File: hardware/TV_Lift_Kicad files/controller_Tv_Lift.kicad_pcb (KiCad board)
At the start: 4 copper layers, 70 x 157.5 mm, 96 parts, among them J1 socket LAN8720a, J10 CONN_IR_OUT, J11 DRY CONTACT UP DOWN, J12 DRY CONTACT, J2 POWER 24V, J3 CAN_bus, J4 ENCODER, J5 ENCODER_POWER, J6 CONN_RS232, J7 M1 LIMIT UP DOWN, J8 Signal PWR, J9 MOTOR_OUT, Q1 2N3904, SW1 UP, SW2 DOWN, SW3 STOP, U1 MAX3232, U10 VNH5019A-E, U2 TSOP32S40F, U3 SN65HVD230, U4 ESP32-WROOM-32, U5 LM2596S-5, U6 AMS1117-3.3, U7 PC817, U8 PC817, U9 NCS1S1205SC

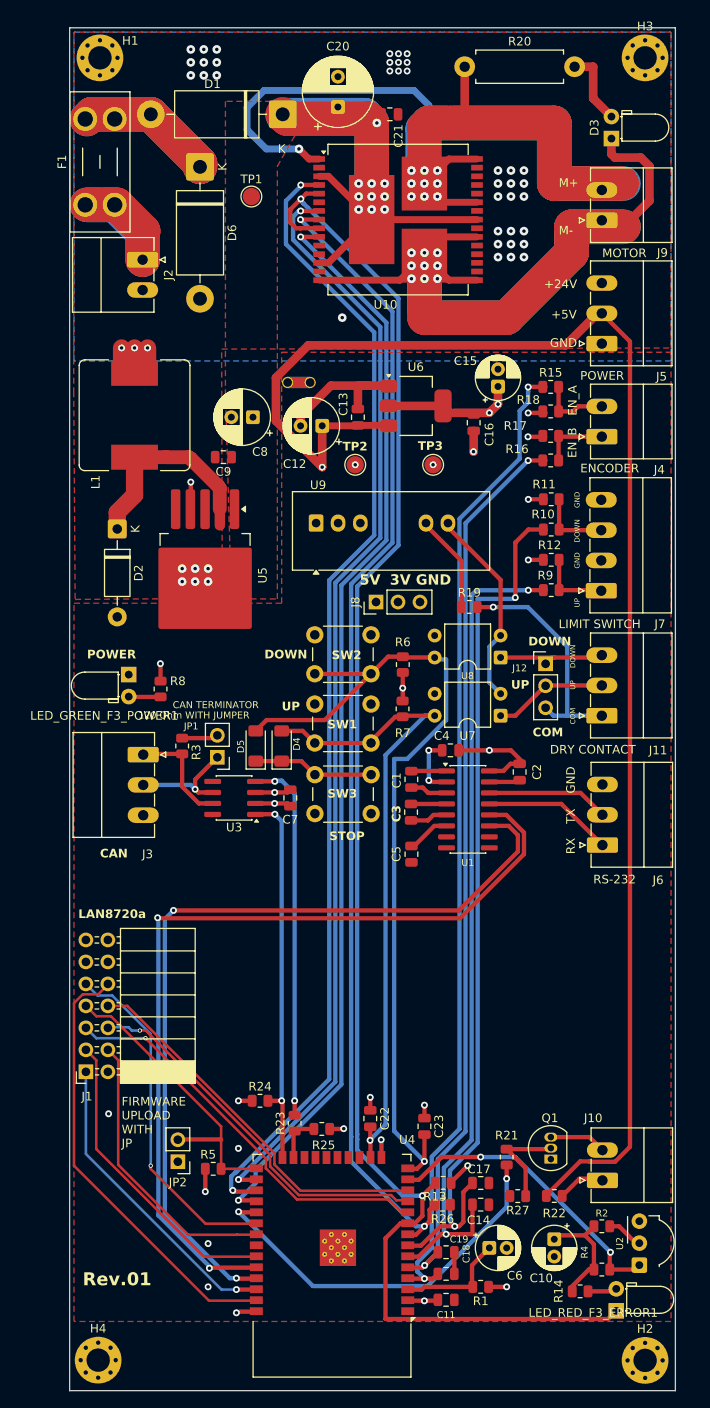
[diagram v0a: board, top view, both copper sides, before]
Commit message: fix schema ( fuse + annotation)
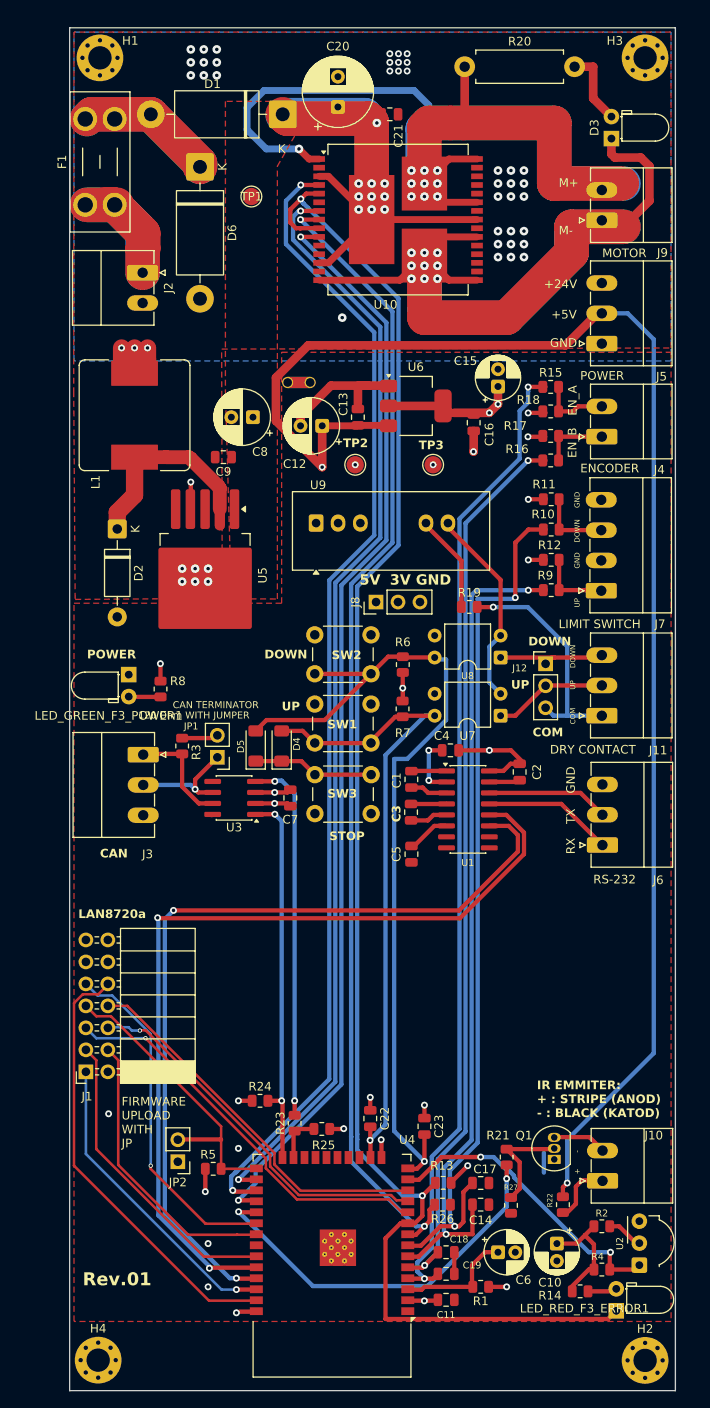
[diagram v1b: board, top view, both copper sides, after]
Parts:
- moved J2 1.50 mm to (73.9, 53.8)
- moved R22 1.41 mm to (122.5, 161.5), turned to -90 degrees
- moved R27 1.33 mm to (116.5, 161.6), turned to -90 degrees
- moved C6 1.12 mm to (115.0, 167.0)
- moved C10 0.59 mm to (121.8, 166.0)
- moved Q1 0.40 mm to (121.5, 156.3)
- moved J10 0.06 mm to (127.1, 158.8)
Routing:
- net Net-(J2-Pin_1): track 34.1 -> 38.7 mm
- net Net-(J10-Pin_2): track 6.58 -> 9.22 mm
- net Net-(J10-Pin_1): track 5.56 -> 7.05 mm
- net +5V: track 187.5 -> 188.4 mm, vias 6 -> 7
- net Net-(U4-EN): track 13.0 -> 13.8 mm
- net +3.3V: track 71.9 -> 72.4 mm
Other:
- board text added: "+"
- board text added: "-"
- board text added: "IR EMMITER: + : STRIPE (ANOD) - : BLACK (KATOD)"

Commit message: fix annotations on sockets output
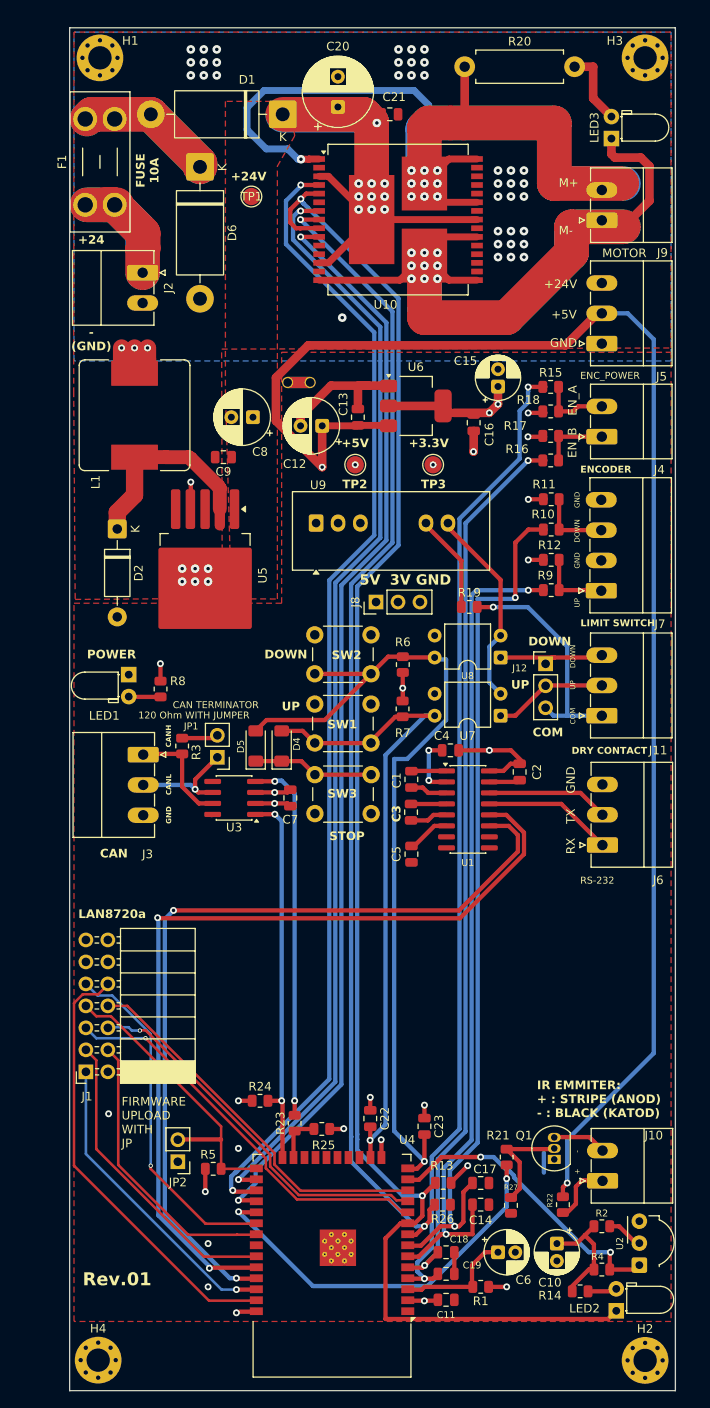
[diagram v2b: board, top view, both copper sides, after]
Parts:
- F1: value Fuse_Small -> Fuse_Mini_10A
- LED1: renamed from LED_GREEN_F3_POWER1; value LED -> LED_GREEN_F3
- LED2: renamed from LED_RED_F3_ERROR1; value LED_ERROR -> LED_RED_F3
- renumbered D3 to LED3
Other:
- board text added: "+24"
- board text added: "+3.3V"
- board text added: "- (GND)"
- board text added: "CANH"
- board text added: "CANL"
- board text added: "ENC_POWER"
- board text added: "FUSE 10A"

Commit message: add button reset
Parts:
- added SW4: Reset, Button_Switch_THT:SW_PUSH_6mm, F.Cu at (67.5, 173.2)
- D1: value 1N5822 -> 80SQ045
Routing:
- net Net-(U4-EN): track 13.8 -> 57.2 mm, vias 0 -> 1
- net Net-(J10-Pin_2): track 9.22 -> 6.92 mm
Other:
- board text added: "Reset"

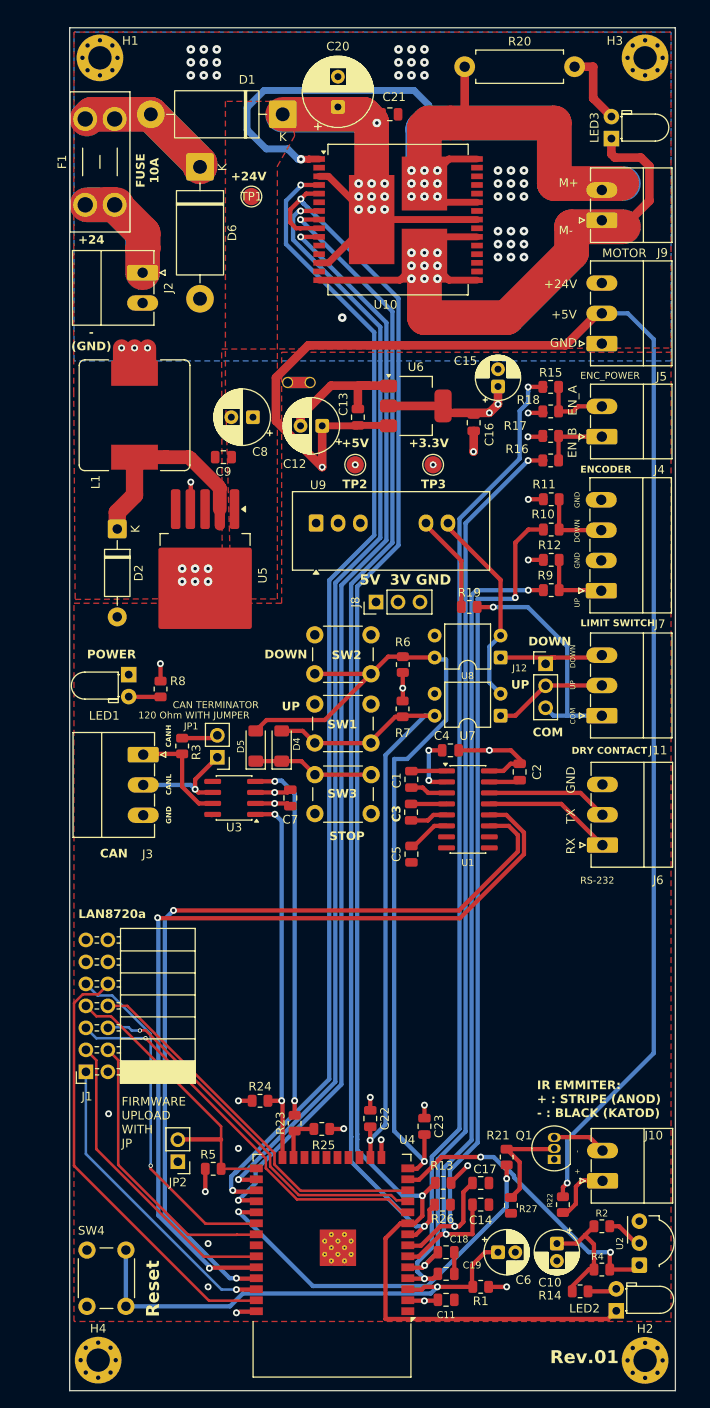
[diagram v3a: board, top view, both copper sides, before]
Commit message: add ground poligon on bottom layer
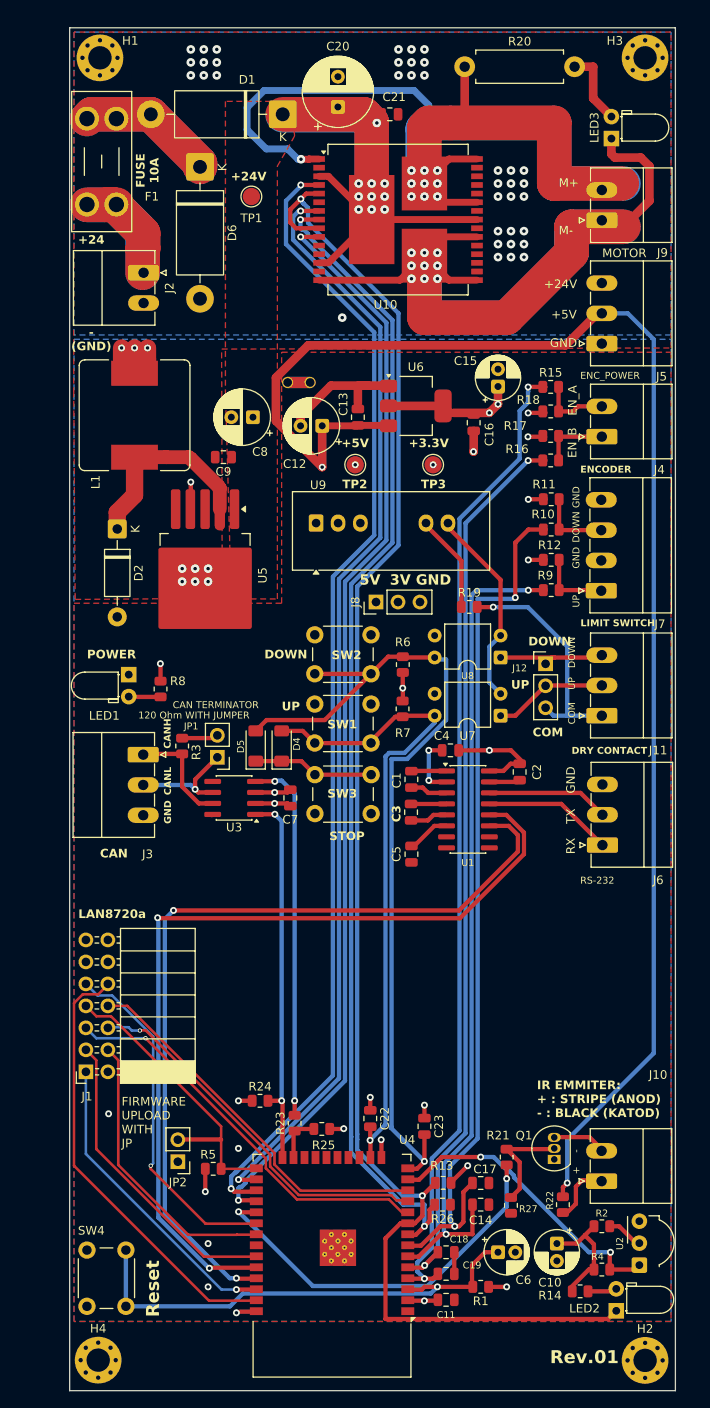
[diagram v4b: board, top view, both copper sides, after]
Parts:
- moved F1 0.20 mm to (67.5, 45.9)
- moved J10 0.11 mm to (127.0, 158.8)
- moved J2 0.11 mm to (74.0, 53.8)
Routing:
- net /M1_CS: track 134.3 -> 135.3 mm
- added copper zone on B.Cu, net GND

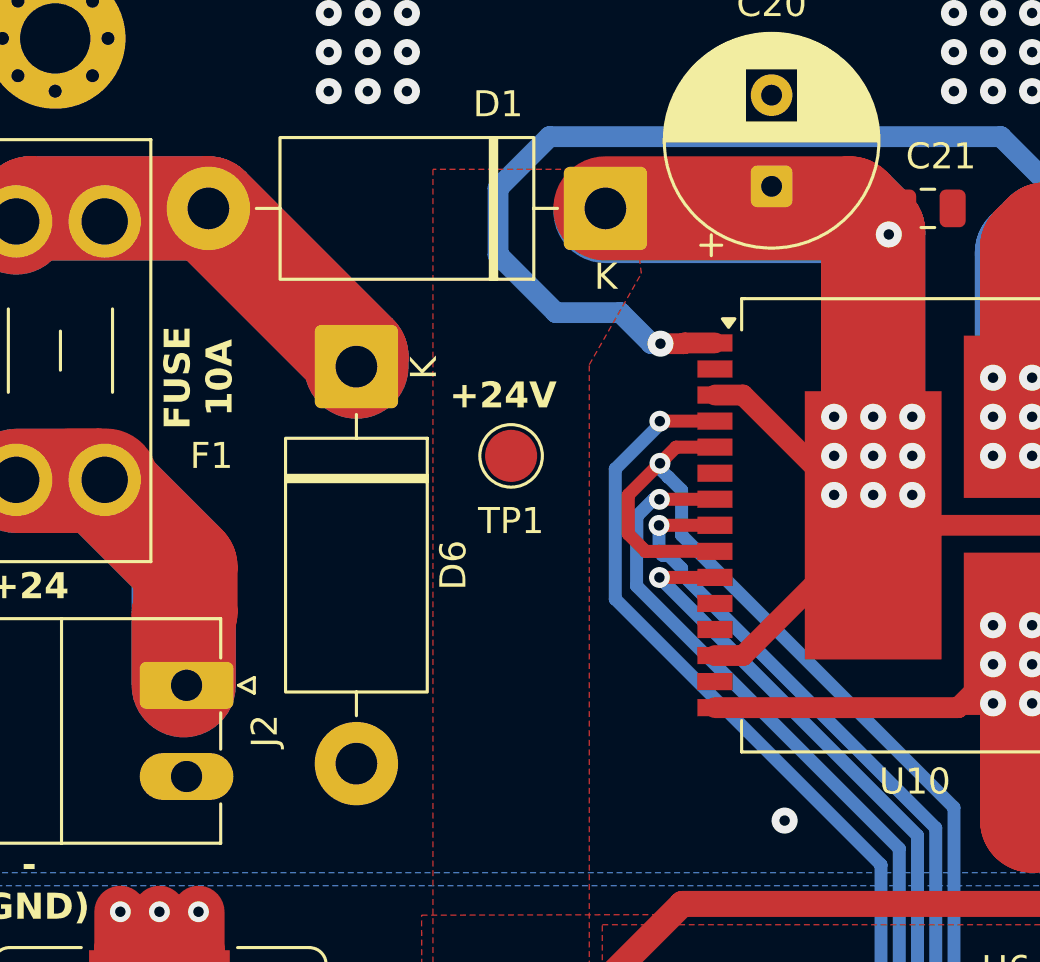
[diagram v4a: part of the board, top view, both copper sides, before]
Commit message: change diod suspressor
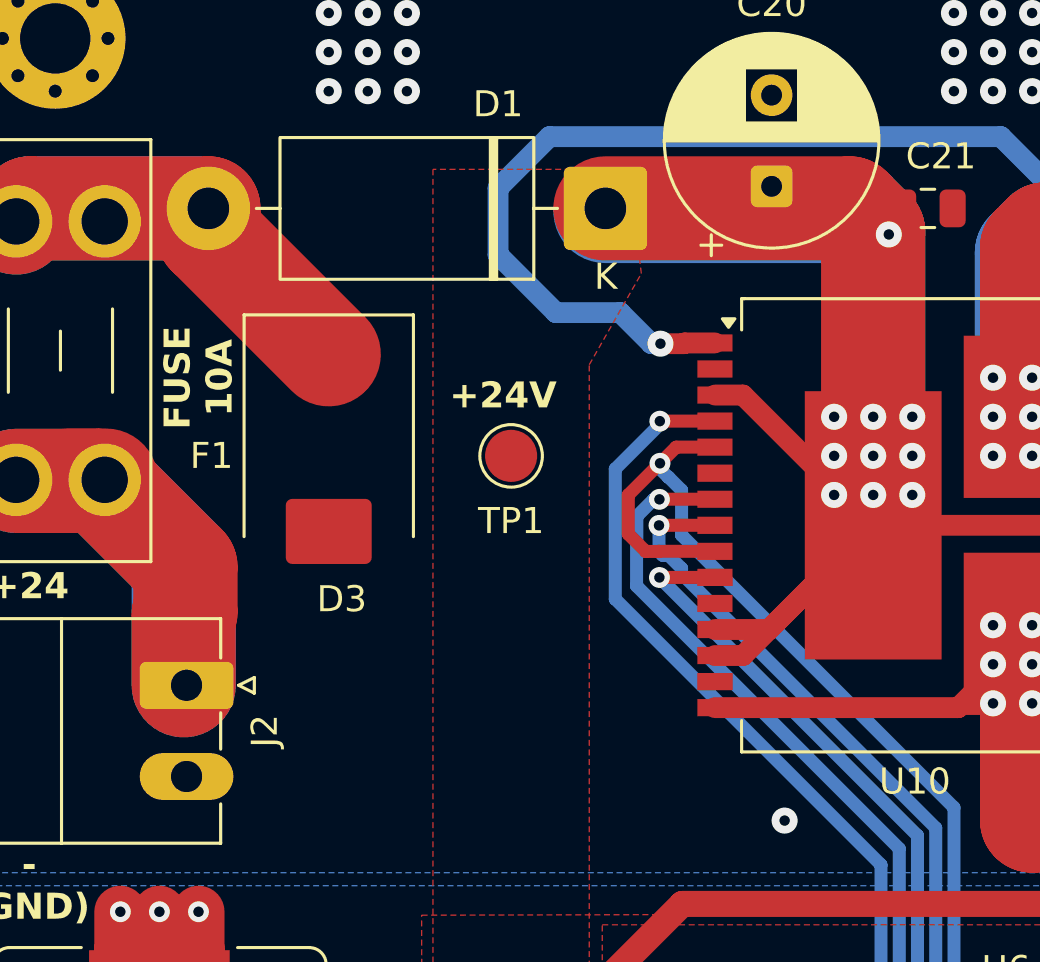
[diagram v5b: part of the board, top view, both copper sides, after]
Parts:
- removed D6: 1.5KE27A, Diode_THT:D_DO-201AD_P15.24mm_Horizontal
- added D3: SMCJ24A, Diode_SMD:D_SMC, F.Cu at (79.5, 44.5)
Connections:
- U10 pad 12: unconnected-(U10-VBAT-Pad12) -> +24V
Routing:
- net Net-(D1-A): track 48.1 -> 30.3 mm
- net +24V: track 88.3 -> 96.0 mm

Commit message: add prodactions file
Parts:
- D1: value 80SQ045 -> 20SQ045
- D3: value SMCJ24A -> SMCJ26A
- J2: footprint Connector_Phoenix_MC:PhoenixContact_MC_1,5_2-G-3.5_1x02_P3.50mm_Horizontal -> Connector_Phoenix_MC_HighVoltage:PhoenixContact_MC_1,5_2-G-5.08_1x02_P5.08mm_Horizontal
- LED2, LED3: footprint LED_THT:LED_D3.0mm_Horizontal_O1.27mm_Z2.0mm -> LED_THT:LED_D3.0mm_Horizontal_O1.27mm_Z6.0mm
- R20: value 2.1k -> 2.4k
- R22: footprint Resistor_SMD:R_0805_2012Metric -> Resistor_SMD:R_1206_3216Metric
- moved R22 2.53 mm to (121.6, 159.1), turned to 0 degrees
- moved J2 0.77 mm to (74.0, 53.0)
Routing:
- net +24V: track 96.0 -> 77.3 mm, vias 10 -> 16
- net +5V: track 188.4 -> 191.5 mm
- net Net-(J10-Pin_1): track 7.05 -> 4.30 mm
